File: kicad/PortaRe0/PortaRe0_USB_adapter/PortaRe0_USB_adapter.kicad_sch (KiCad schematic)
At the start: 4 parts, among them J7 FPC_USB_3.1, J8 FPC_USB_2.0

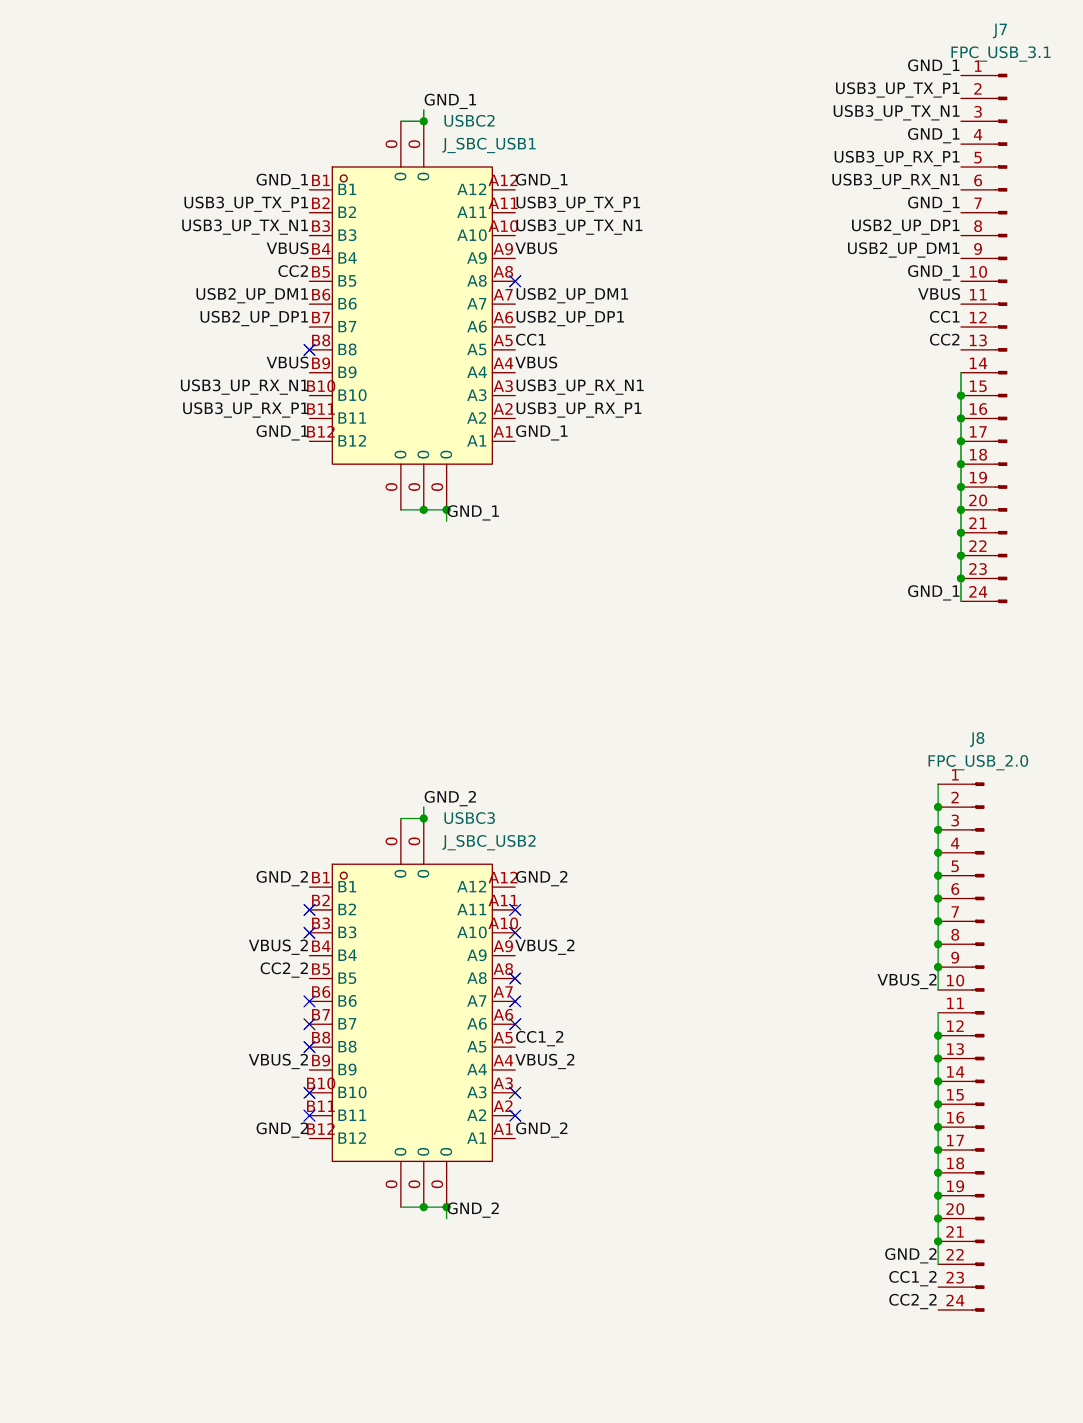
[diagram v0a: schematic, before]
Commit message: Docs: session40終了処理・メインPCB完了・hdmi_adapter/usb_adapter(FPC)完了・software/フォルダ作成
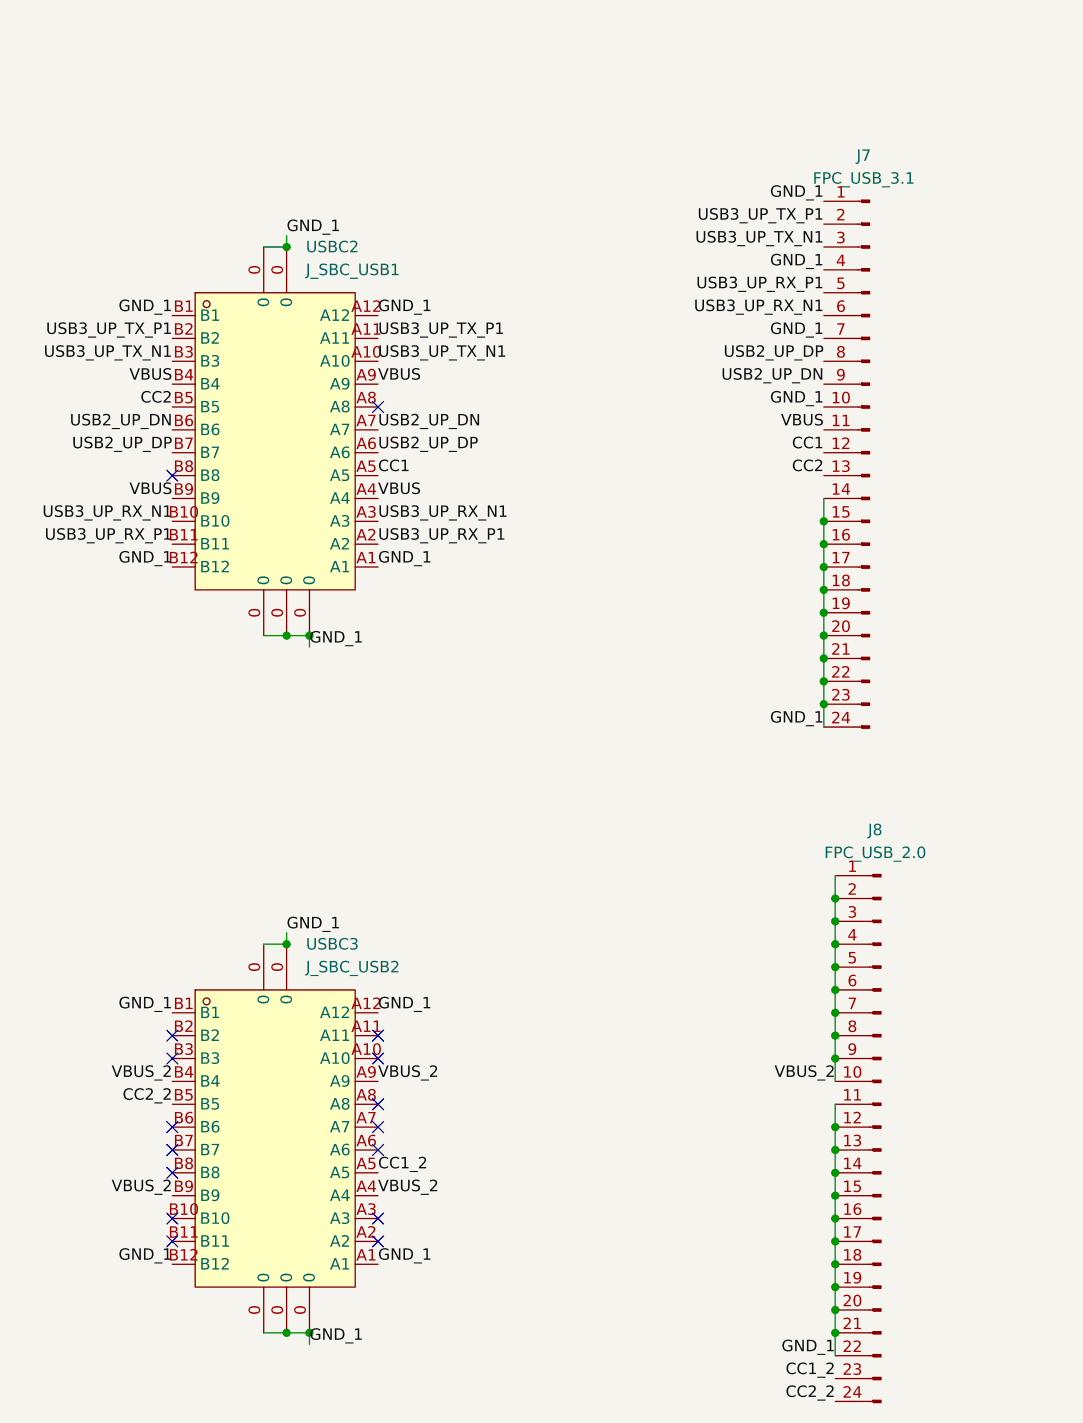
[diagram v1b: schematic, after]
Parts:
- J7: footprint (none) -> PortaRe0:FPC-24P-0.5mm
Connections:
- net GND_2 is gone; now on net GND_1: J8.11 (Pin_11), J8.12 (Pin_12), J8.13 (Pin_13), J8.14 (Pin_14), J8.15 (Pin_15), J8.16 (Pin_16), J8.17 (Pin_17), J8.18 (Pin_18), J8.19 (Pin_19), J8.20 (Pin_20), J8.21 (Pin_21), J8.22 (Pin_22), USBC3.0, USBC3.A1, USBC3.A12, USBC3.B1, USBC3.B12
- net USB2_UP_DM1 renamed USB2_UP_DN
- net USB2_UP_DP1 renamed USB2_UP_DP
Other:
- moved on the sheet: J7, J8, USBC2, USBC3
